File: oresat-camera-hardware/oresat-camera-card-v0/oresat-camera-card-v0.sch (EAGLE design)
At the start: 308 parts, among them J2 2-1734592-0, J5 DM3BT-DSF-PEJS, J6 J-SAMTEC-TFM-120-X1-XXX-D-RA, J8 3-1734592-64-1734592-0, Q1 DMP2240UDM, Q2 MMBT2907, Q3 MOSFET-PCH-SOT23-6, Q4 MOSFET-PCH-SOT23-6, Q5 PMV45EN, Q6 PMV45EN, Q7 DMP2240UDM, U1 OSD3358-512M-BSM, U11 SN74LVC8T245MPWREPPW24-M, U12 TCA9509DGKRDGK8-M, U13 TLVH431, U14 RCLAMP0504FB, U15 TLV70028QDDCRQ1, U16 RCLAMP0504FB, U2 TCAN330, U3 MAX7310ATE, U4 MAX4211CETE, U5 TPS62112, U6 CLVCH16T245MDGGREP, U8 SN74LVC1G07DCK, U9 TPS2051CDBVR, Y2 24MHz

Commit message: first draft finished
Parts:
- removed C40, C41, C42, C43: 0.1uF, oresat-rcl:C-EU0603-A-NOSILK
- removed D9: BLUE, SparkFun-LED:LED-BLUE0603
- removed J14: (no value), SparkFun-Connectors:CONN_03LONGPADS
- removed J15: (no value), SparkFun-Connectors:CONN_02PTH3
- removed U$2, U$4: MIC842, Q-Microchip-MIC842-Comparator:MIC842
- removed U16: RCLAMP0504FB, U-Semtec-RCLAMP0504FB:RCLAMP0504FB
- added C19, C20: 1uF, oresat-rcl:C-EU0603-A-NOSILK
- added C34: 0.1uF, oresat-rcl:C-EU0603-A-NOSILK
- added C8: 22u, oresat-rcl:C-EU0805-B-NOSILK
- added D3: GREEN, SparkFun-LED:LED-GREEN0603
- added J1: J-SAMTEC-TFM-120-X1-XXX-D-RA, J-Samtec-TFM-120-X1-XXX-D-RA:J-SAMTEC-TFM-120-X1-XXX-D-RA
- added J4: 3-1734592-64-1734592-0, J-TEConnectivity-X-1734592-X:3-1734592-64-1734592-0
- added JP7: JUMPER-SMT_3_1-NC_TRACE_SILK, SparkFun-Jumpers:JUMPER-SMT_3_1-NC_TRACE_SILK
- added Q8: PMV45EN, Tova:PMV45EN
- added TP143, TP144: TEST-POINT3X4, SparkFun-Connectors:TEST-POINT3X4
- added U7: TCA9509DGKRDGK8-M, U-TI-TCA9509DGKR-I2C_repeater:TCA9509DGKRDGK8-M
- C1: value 100n -> NP; device rcl_custom:C-EU0402-B-NOSILK -> oresat-rcl:C-EU0805-B-NOSILK; DIS Digi-Key -> (none); DPN 1276-1001-1-ND -> (none); MFR Samsung -> (none); MPN CL05B104KO5NNNC -> (none)
- C10: value 1u -> 0.1uF; DIS Digi-Key -> (none); DPN 1276-1001-1-ND -> (none); MFR Samsung -> (none); MPN CL05B104KO5NNNC -> (none)
- C11: DIS (none) -> Digi-Key; DPN (none) -> 1276-1001-1-ND; MFR (none) -> Samsung; MPN (none) -> CL05B104KO5NNNC
- C12: value 22u -> 0.1uF; device oresat-rcl:C-EU0805-B-NOSILK -> oresat-rcl:C-EU0603-A-NOSILK
- C13: value 22uF -> 0.1uF; device oresat-rcl:C-EUC1210 -> oresat-rcl:C-EU0603-A-NOSILK
- C14: value 0.1uF, 6.3V -> 0.1uF
- C15: value 18pF, 50V -> 0.1uF
- C17: DIS Digi-Key -> (none); DPN 1276-1001-1-ND -> (none); MFR Samsung -> (none); MPN CL05B104KO5NNNC -> (none)
- C18: value 18pF, 50V -> 2.2uF
- C2: device oresat-rcl:C-EU0603-A-NOSILK -> oresat-rcl:C-EU0805-B-NOSILK; DIS Digi-Key -> (none); DPN 1276-1001-1-ND -> (none); MFR Samsung -> (none); MPN CL05B104KO5NNNC -> (none)
- C21, C26: value 0.1uF -> 1uF
- C22: value 22uF -> 1uF; device oresat-rcl:C-EUC1210 -> oresat-rcl:C-EU0603-A-NOSILK
- C23: value 0.1uF -> 10uF
- C24, C27, C33: value 10uF -> 0.1uF
- C25: value 10uF -> 1uF
- C28: value 2.2uF -> 18pF, 50V
- C29: value 1uF -> 18pF, 50V
- C3: value 0.1uF -> 100n; DIS (none) -> Digi-Key; DPN (none) -> 1276-1001-1-ND; MFR (none) -> Samsung; MPN (none) -> CL05B104KO5NNNC
- C30, C32: value 1uF -> 0.1uF
- C31: value 1uF -> 1nF
- C35, C36: value 1uF -> 10uF
- C37, C38: value 0.1uF -> 22uF; device oresat-rcl:C-EU0603-A-NOSILK -> oresat-rcl:C-EUC1210
- C39: value 0.1uF -> 0.1uF, 6.3V
- C4: value NP -> 10u
- C6: value NP -> 1u; device oresat-rcl:C-EU0805-B-NOSILK -> oresat-rcl:C-EU0603-A-NOSILK; DIS (none) -> Digi-Key; DPN (none) -> 1276-1001-1-ND; MFR (none) -> Samsung; MPN (none) -> CL05B104KO5NNNC
- C7: value 10u -> NP; device oresat-rcl:C-EU0805-B-NOSILK -> oresat-rcl:C-EU0603-A-NOSILK; DIS (none) -> Digi-Key; DPN (none) -> 1276-1001-1-ND; MFR (none) -> Samsung; MPN (none) -> CL05B104KO5NNNC
- C9: value 1nF -> 10uF
- D1: value GREEN -> AMBER
- D4: value AMBER -> BLUE; device SparkFun-LED:LED-GREEN0603 -> SparkFun-LED:LED-BLUE0603
- D5: value GREEN -> BLUE; device SparkFun-LED:LED-GREEN0603 -> SparkFun-LED:LED-BLUE0603
- D8: value BLUE -> GREEN; device SparkFun-LED:LED-BLUE0603 -> SparkFun-LED:LED-GREEN0603
- J10, J11: device SparkFun-Connectors:CONN_05 -> SparkFun-Connectors:CONN_02PTH3
- J2: value 2-1734592-0 -> DM3BT-DSF-PEJS; device J-TEConnectivity-X-1734592-X:2-1734592-0 -> J-Hirose-DM3BT-DSF-PEJS:DM3BT-DSF-PEJS
- J3: device SparkFun-Connectors:CONN_02PTH3 -> SparkFun-Connectors:CONN_03LONGPADS
- J5: value DM3BT-DSF-PEJS -> (none); device J-Hirose-DM3BT-DSF-PEJS:DM3BT-DSF-PEJS -> SparkFun-Connectors:CONN_05
- J6: value J-SAMTEC-TFM-120-X1-XXX-D-RA -> (none); device J-Samtec-TFM-120-X1-XXX-D-RA:J-SAMTEC-TFM-120-X1-XXX-D-RA -> SparkFun-Connectors:CONN_05; MFR Samtec -> (none); MPN TFM-120-01-L-D-RA -> (none)
- J8: value 3-1734592-64-1734592-0 -> 2-1734592-0; device J-TEConnectivity-X-1734592-X:3-1734592-64-1734592-0 -> J-TEConnectivity-X-1734592-X:2-1734592-0
- Q3, Q4: value MOSFET-PCH-SOT23-6 -> MIC842; device Q-MOSFET-PCH-SOT23-6:MOSFET-PCH-SOT23-6 -> Q-Microchip-MIC842-Comparator:MIC842; MFR Diodes Inc -> (none); MPN DMP3050LVT-7 -> (none)
- Q6: value PMV45EN -> MOSFET-PCH-SOT23-6; device Tova:PMV45EN -> Q-MOSFET-PCH-SOT23-6:MOSFET-PCH-SOT23-6; MFR (none) -> Diodes Inc; MPN (none) -> DMP3050LVT-7
- Q7: value DMP2240UDM -> MOSFET-PCH-SOT23-6; device Q-MOSFET-PCH-dual-SOT23-6:MOSFET-PCH-SOT23-6 -> Q-MOSFET-PCH-SOT23-6:MOSFET-PCH-SOT23-6; MPN DMP2240UDM -> DMP3050LVT-7
- R1: value 2.7k -> 100; device rcl_custom:R-US_0402-B-NOSILK -> oresat-rcl:R-US_0603-A-NOSILK
- R11, R14, R5, R8, R9: device rcl_custom:R-US_0402-B-NOSILK -> oresat-rcl:R-US_0603-A-NOSILK
- R12: value 2.7k -> 10k; device rcl_custom:R-US_0402-B-NOSILK -> oresat-rcl:R-US_0603-A-NOSILK
- R13: value NP -> 10k; device rcl_custom:R-US_0402-B-NOSILK -> oresat-rcl:R-US_0603-A-NOSILK
- R15: value 10k -> NP; device rcl_custom:R-US_0402-B-NOSILK -> oresat-rcl:R-US_0603-A-NOSILK
- R16: value 47k -> NP; device rcl_custom:R-US_0402-B-NOSILK -> oresat-rcl:R-US_0603-A-NOSILK
- R17, R3: value 0 -> NP; DIS (none) -> Digi-Key; DPN (none) -> 1276-4275-1-ND; MFR (none) -> Samsung; MPN (none) -> RC1005F6653CS
- R18: value 47k -> 10k; device rcl_custom:R-US_0402-B-NOSILK -> oresat-rcl:R-US_0603-A-NOSILK
- R19, R20, R21, R22: value NP -> TBD; device rcl_custom:R-US_0402-B-NOSILK -> oresat-rcl:R-US_0603-A-NOSILK
- R2: value 2.7k -> NP; device rcl_custom:R-US_0402-B-NOSILK -> oresat-rcl:R-US_0603-A-NOSILK
- R23, R24: value NP -> 47k; device rcl_custom:R-US_0402-B-NOSILK -> oresat-rcl:R-US_0603-A-NOSILK
- R25: value 100 -> 10k; device rcl_custom:R-US_0402-B-NOSILK -> oresat-rcl:R-US_0603-A-NOSILK
- R26: value 10k -> 2.7k; device rcl_custom:R-US_0402-B-NOSILK -> oresat-rcl:R-US_0603-A-NOSILK
- R29: value 100m -> NP; device rcl:R-US_R1206 -> oresat-rcl:R-US_0603-A-NOSILK; DIS (none) -> Digi-Key; DPN (none) -> 1276-4275-1-ND; MFR (none) -> Samsung; MPN (none) -> RC1005F6653CS
- R30, R38: value 10k -> NP
- R31: value 0 -> NP
- R32: value NP -> 100m; device oresat-rcl:R-US_0603-A-NOSILK -> rcl:R-US_R1206; DIS Digi-Key -> (none); DPN 1276-4275-1-ND -> (none); MFR Samsung -> (none); MPN RC1005F6653CS -> (none)
- R33: value 0 -> 2.7k
- R34: value NP -> 10k
- R35, R63, R64: value 10k -> 0
- R36: value NP -> 0
- R39: value 1k -> 10k; device oresat-rcl:R-US_0603-A -> oresat-rcl:R-US_0603-A-NOSILK; DIS (none) -> Digi-Key; DPN (none) -> 1276-4275-1-ND; MFR (none) -> Samsung; MPN (none) -> RC1005F6653CS
- R4: value 100 -> NP; device rcl_custom:R-US_0402-B-NOSILK -> oresat-rcl:R-US_0603-A-NOSILK
- R40: value 1M, 1% -> 10k; device oresat-rcl:R-US_0603-A -> oresat-rcl:R-US_0603-A-NOSILK; DIS (none) -> Digi-Key; DPN (none) -> 1276-4275-1-ND; MFR (none) -> Samsung; MPN (none) -> RC1005F6653CS
- R41: value 10K -> 2.7k; device R-Panasonic-EXB_A10PXXXJ:EXB-A10P391JC_ARRAY_EXBA-M -> oresat-rcl:R-US_0603-A-NOSILK; DIS (none) -> Digi-Key; DPN (none) -> 1276-4275-1-ND; MFR (none) -> Samsung; MPN (none) -> RC1005F6653CS
- R42: value 1k -> 10K; device oresat-rcl:R-US_0603-A -> R-Panasonic-EXB_A10PXXXJ:EXB-A10P391JC_ARRAY_EXBA-M
- R43, R44: value 1k -> 4.7k; device oresat-rcl:R-US_0603-A -> oresat-rcl:R-US_0603-A-NOSILK
- R45: value 1k -> 10k; device oresat-rcl:R-US_0603-A -> oresat-rcl:R-US_0603-A-NOSILK
- R46, R47: device oresat-rcl:R-US_0603-A -> oresat-rcl:R-US_0603-A-NOSILK
- R48: value 10k -> 10K; device oresat-rcl:R-US_0603-A -> R-Panasonic-EXB_A10PXXXJ:EXB-A10P391JC_ARRAY_EXBA-M
- R49: value 10k -> 1k
- R50: value 10K -> 1k; device R-Panasonic-EXB_A10PXXXJ:EXB-A10P391JC_ARRAY_EXBA-M -> oresat-rcl:R-US_0603-A
- R51, R52: value 100K -> 1k; device R-Panasonic-EXB_A10PXXXJ:EXB-A10P391JC_ARRAY_EXBA-M -> oresat-rcl:R-US_0603-A
- R53: value 100K -> 10K
- R54: value NP -> 4.7k; device rcl_custom:R-US_0402-B-NOSILK -> oresat-rcl:R-US_0603-A-NOSILK; DIS Digi-Key -> (none); DPN 1276-4275-1-ND -> (none); MFR Samsung -> (none); MPN RC1005F6653CS -> (none)
- R55: value 4.75K -> 4.7k
- R56: value 4.75K -> 10k
- R58: value 10k -> 100K; device oresat-rcl:R-US_0603-A-NOSILK -> R-Panasonic-EXB_A10PXXXJ:EXB-A10P391JC_ARRAY_EXBA-M
- R59, R60: value 4.7k -> 100K; device oresat-rcl:R-US_0603-A-NOSILK -> R-Panasonic-EXB_A10PXXXJ:EXB-A10P391JC_ARRAY_EXBA-M
- R6: value NP -> 100; device rcl_custom:R-US_0402-B-NOSILK -> oresat-rcl:R-US_0603-A-NOSILK
- R61: value 4.7k -> 10k; device oresat-rcl:R-US_0603-A-NOSILK -> oresat-rcl:R-US_0603-A
- R62: value 4.7k -> 1M, 1%; device oresat-rcl:R-US_0603-A-NOSILK -> oresat-rcl:R-US_0603-A
- R65: value 10k -> 4.75K
- R66: value 10.0K -> 4.75K; device oresat-rcl:R-US_0603-A -> oresat-rcl:R-US_0603-A-NOSILK
- R67: value 40.2K -> 10k
- R68: value 499 -> 10k
- R69: value 10K -> 10k; device R-Panasonic-EXB_A10PXXXJ:EXB-A10P391JC_ARRAY_EXBA-M -> oresat-rcl:R-US_0603-A
- R7: value 10k -> 100
- R70: value 100 -> 1k; device rcl_custom:R-US_0402-B-NOSILK -> oresat-rcl:R-US_0603-A; DIS Digi-Key -> (none); DPN 1276-4275-1-ND -> (none); MFR Samsung -> (none); MPN RC1005F6653CS -> (none)
- R71: value 10k -> 499; device rcl_custom:R-US_0402-B-NOSILK -> oresat-rcl:R-US_0603-A; DIS Digi-Key -> (none); DPN 1276-4275-1-ND -> (none); MFR Samsung -> (none); MPN RC1005F6653CS -> (none)
- R72: value NP -> 40.2K; device rcl_custom:R-US_0402-B-NOSILK -> oresat-rcl:R-US_0603-A; DIS Digi-Key -> (none); DPN 1276-4275-1-ND -> (none); MFR Samsung -> (none); MPN RC1005F6653CS -> (none)
- R73: value NP -> 10.0K; device rcl_custom:R-US_0402-B-NOSILK -> oresat-rcl:R-US_0603-A; DIS Digi-Key -> (none); DPN 1276-4275-1-ND -> (none); MFR Samsung -> (none); MPN RC1005F6653CS -> (none)
- TP142: value TEST-POINT -> TEST-POINT3X4; device Tova:TEST-POINT -> SparkFun-Connectors:TEST-POINT3X4
- TP15: value TEST-POINT3X4 -> TEST-POINT; device SparkFun-Connectors:TEST-POINT3X4 -> Tova:TEST-POINT
- U1: value OSD3358-512M-BSM -> MAX7310ATE; device U-OSD3358-512M-BSM:OSD3358-512M-BSM -> U-Maxim-MAX7310-I2C-GPIO-expander:MAX7310; MFR (none) -> Maxim; MPN (none) -> MAX7310ATE
- U10: value (none) -> SN74LVC8T245MPWREPPW24-M; device U-Generic-eMMC-153pin:EMMC+RESET-BA -> U-TI-SN74LVC8T245MPWREP-8bit-TRX:SN74LVC8T245MPWREPPW24-M
- U11: value SN74LVC8T245MPWREPPW24-M -> RCLAMP0504FB; device U-TI-SN74LVC8T245MPWREP-8bit-TRX:SN74LVC8T245MPWREPPW24-M -> U-Semtec-RCLAMP0504FB:RCLAMP0504FB
- U12: value TCA9509DGKRDGK8-M -> RCLAMP0504FB; device U-TI-TCA9509DGKR-I2C_repeater:TCA9509DGKRDGK8-M -> U-Semtec-RCLAMP0504FB:RCLAMP0504FB
- U13: value TLVH431 -> TPS2051CDBVR; device U-TI-TLVH431-Shunt-Regulator:TLVH431 -> U-TI-TPS2051C:TPS2051CDBVR
- U14: value RCLAMP0504FB -> TLVH431; device U-Semtec-RCLAMP0504FB:RCLAMP0504FB -> U-TI-TLVH431-Shunt-Regulator:TLVH431
- U15: value TLV70028QDDCRQ1 -> SN74LVC1G07DCK; device U-TI-TLV70028QDDCRQ1-VoltageReg:TLV70028QDDCRQ1 -> U-TI-SN74LVC1G07DCK-Buffer:SN74LVC1G07DCK
- U2: value TCAN330 -> TPS62112; device U-TI-TCAN330-CAN-transceiver:TCAN330 -> U-TI-TPS6211x-SPS-buck:TPS6211X; MFR Texas Instruments -> TI; MPN TCAN330GDCNT -> TPS62111RSA
- U3: value MAX7310ATE -> MAX4211CETE; device U-Maxim-MAX7310-I2C-GPIO-expander:MAX7310 -> U-Maxim-MAX4211-power-monitor:MAX4211; MPN MAX7310ATE -> MAX4211CETE
- U4: value MAX4211CETE -> TCAN330; device U-Maxim-MAX4211-power-monitor:MAX4211 -> U-TI-TCAN330-CAN-transceiver:TCAN330; MFR Maxim -> Texas Instruments; MPN MAX4211CETE -> TCAN330GDCNT
- U5: value TPS62112 -> CLVCH16T245MDGGREP; device U-TI-TPS6211x-SPS-buck:TPS6211X -> U-TI-CLVCH16T245MDGxREP-16bit-TRX:CLVCH16T245MDGGREP; MFR TI -> (none); MPN TPS62111RSA -> (none)
- U6: value CLVCH16T245MDGGREP -> OSD3358-512M-BSM; device U-TI-CLVCH16T245MDGxREP-16bit-TRX:CLVCH16T245MDGGREP -> U-OSD3358-512M-BSM:OSD3358-512M-BSM
- U8: value SN74LVC1G07DCK -> (none); device U-TI-SN74LVC1G07DCK-Buffer:SN74LVC1G07DCK -> U-Generic-eMMC-153pin:EMMC+RESET-BA
- U9: value TPS2051CDBVR -> TLV70028QDDCRQ1; device U-TI-TPS2051C:TPS2051CDBVR -> U-TI-TLV70028QDDCRQ1-VoltageReg:TLV70028QDDCRQ1
- renumbered C44 to C16, CM4 to CM1, J12 to J7, J13 to J9, L2 to L1, Q2 to Q9, Y2 to Y1
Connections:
- new net N$100: C2.1, Q4.CIN, R20.1, R22.1
- new net N$101: C1.1, Q3.CIN, R19.1, R21.1
- new net N$102: JP7.2, U6B.USB1_ID
- new net USB_HO_ID: J8.4, JP7.1
- net !FAULT: now also Q8.D, R40.1, TP10.1, U1.IO2; no longer Q6.D, R38.1, TP8.1, U3.IO2
- net !OE_E: now also J4.26, U10.A5; no longer J8.26, U11.A5
- net !RESET_E: now also J4.24, U10.A3; no longer J8.24, U11.A3
- net !SD: now also J1.39, J1.40; no longer J6.39, J6.40
- net 2.8V: now also C14.1, C15.1, C17.1, C24.1, C26.1, R54.1, R55.1, U10.VCCA, U5.VCCB, U7.VCCB, U9.OUT; no longer C36.1, C39.1, C40.1, C41.1, C43.1, R59.1, R60.1, U11.VCCA, U12.VCCB, U15.OUT, U6.VCCB
- net 3.3V: now also C10.1, C11.2, C12.1, C13.1, C19.1, C20.1, C21.1, C22.1, C23.1, C25.1, C9.1, J2.VDD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; no longer C17.2, C26.1, C29.1, C30.1, C31.1, C32.1, C33.1, C35.1, C37.1, C38.1, C42.1, J5.VDD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
- net 5V: now also C8.1, R33.2, TP15.1, U2.FB; no longer C12.1, R2.2, TP17.1, U5.FB
- net 5V_IN: now also C37.1, U6A.VIN_AC@1, U6A.VIN_AC@2, U6A.VIN_AC@3; no longer C13.1, U1A.VIN_AC@1, U1A.VIN_AC@2, U1A.VIN_AC@3
- net AD0: now also R14.2, R15.1, R16.1, R17.2, U1.AD0; no longer R5.1, R6.2, R8.2, R9.1, U3.AD0
- net AD1: now also R10.1, R11.2, R8.2, R9.1, U1.AD1; no longer R11.1, R13.2, R14.2, R19.1, U3.AD1
- net AD2: now also R2.2, R3.1, R4.1, R5.2, U1.AD2; no longer R20.1, R21.2, R22.2, R23.1, U3.AD2
- net AGND: now also C31.2, C33.2, C34.2, R64.2, U6B.AGND_ADC; no longer C11.2, C3.2, C9.2, R17.2, U1B.AGND_ADC
- net BOOT0: now also U1.IO5; no longer U3.IO5
- net BUS_OE: now also R45.1, TP80.1, U5.!1OE, U5.!2OE, U6D.MII1_CRS; no longer R58.1, TP96.1, U1D.MII1_CRS, U6.!1OE, U6.!2OE
- net CAM_OE: now also TP81.1, U10.B5, U6D.MII1_COL; no longer TP97.1, U11.B5, U1D.MII1_COL
- net CAN1_H: now also J1.33, J1.34, TP143.1; no longer J6.33, J6.34
- net CAN1_L: now also J1.35, J1.36, TP144.1; no longer J6.35, J6.36
- net CAN2_H: now also J1.17, J1.18, U4.CANH; no longer J6.17, J6.18, U2.CANH
- net CAN2_L: now also J1.19, J1.20, U4.CANL; no longer J6.19, J6.20, U2.CANL
- net CB-RESET: now also R34.2, TP18.1, U1.IO4, U3.CIN2-; no longer R30.2, TP14.1, U3.IO4, U4.CIN2-
- net CB_CTRL: now also Q7.G, Q8.G, R39.1, TP14.1, U3.COUT1, U3.COUT2, U3.LE; no longer Q3.G, Q6.G, R35.1, TP3.1, U4.COUT1, U4.COUT2, U4.LE
- net CLK_EN: now also TP82.1, U10.B2, U6D.MII1_RX_CLK; no longer TP98.1, U11.B2, U1D.MII1_RX_CLK
- net CLK_EN_E: now also J4.23, U10.A2; no longer J8.23, U11.A2
- net D0_E: now also J4.12, U5.1B7; no longer J8.12, U6.1B7
- net D0_I: now also JP1.1, TP32.1, U5.1A7; no longer JP4.1, TP108.1, U6.1A7
- net D10_E: now also J4.16, U5.1B3; no longer J8.16, U6.1B3
- net D10_I: now also TP42.1, U5.1A3, U6C.MCASP0_AXR1; no longer TP118.1, U1C.MCASP0_AXR1, U6.1A3
- net D11_E: now also J4.17, U5.1B2; no longer J8.17, U6.1B2
- net D11_I: now also TP43.1, U5.1A2, U6C.MCASP0_AHCLKX; no longer TP119.1, U1C.MCASP0_AHCLKX, U6.1A2
- net D1_E: now also J4.11, U5.1B8; no longer J8.11, U6.1B8
- net D1_I: now also JP2.1, TP33.1, U5.1A8; no longer JP3.1, TP109.1, U6.1A8
- net D2_E: now also J4.10, U5.2B1; no longer J8.10, U6.2B1
- net D2_I: now also JP3.1, TP34.1, U5.2A1; no longer JP2.1, TP110.1, U6.2A1
- net D3_E: now also J4.9, U5.2B2; no longer J8.9, U6.2B2
- net D3_I: now also JP4.1, TP35.1, U5.2A2; no longer JP1.1, TP111.1, U6.2A2
- net D4_E: now also J4.8, U5.2B3; no longer J8.8, U6.2B3
- net D4_I: now also TP36.1, U5.2A3, U6C.MCASP0_ACLKX; no longer TP112.1, U1C.MCASP0_ACLKX, U6.2A3
- net D5_E: now also J4.7, U5.2B4; no longer J8.7, U6.2B4
- net D5_I: now also TP37.1, U5.2A4, U6C.MCASP0_FSX; no longer TP113.1, U1C.MCASP0_FSX, U6.2A4
- net D6_E: now also J4.6, U5.2B5; no longer J8.6, U6.2B5
- net D6_I: now also TP38.1, U5.2A5, U6C.MCASP0_AXR0; no longer TP114.1, U1C.MCASP0_AXR0, U6.2A5
- net D7_E: now also J4.13, U5.1B6; no longer J8.13, U6.1B6
- net D7_I: now also TP39.1, U5.1A6, U6C.MCASP0_AHCLKR; no longer TP115.1, U1C.MCASP0_AHCLKR, U6.1A6
- net D8_E: now also J4.14, U5.1B5; no longer J8.14, U6.1B5
- net D8_I: now also TP40.1, U5.1A5, U6C.MCASP0_ACLKR; no longer TP116.1, U1C.MCASP0_ACLKR, U6.1A5
- net D9_E: now also J4.15, U5.1B4; no longer J8.15, U6.1B4
- net D9_I: now also TP41.1, U5.1A4, U6C.MCASP0_FSR; no longer TP117.1, U1C.MCASP0_FSR, U6.1A4
- net FLASH: now also TP83.1, U5.1A1, U6D.MII1_TXD3; no longer TP99.1, U1D.MII1_TXD3, U6.1A1
- net FLASH_E: now also J4.28, U5.1B1; no longer J8.28, U6.1B1
- net GND: now also C1.2, C11.1, C15.2, C17.2, C18.2, C19.2, C2.2, C20.2, C3.1, C8.2, C9.2, D3.C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; no longer C1.1, C17.1, C28.2, C29.2, C31.2, C33.2, C40.2, C41.2, C42.2, C43.2, C7.2, D9.C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
- net HSYNC_E: now also J4.4, U5.2B7; no longer J8.4, U6.2B7
- net HSYNC_I: now also TP44.1, U5.2A7, U6C.GPMC_AD15; no longer TP120.1, U1C.GPMC_AD15, U6.2A7
- net I2C2_SCL: now also J4.21, R54.2, U7.SCLB; no longer J8.21, R60.2, U12.SCLB
- net I2C2_SDA: now also J4.22, R55.2, U7.SDAB; no longer J8.22, R59.2, U12.SDAB
- net INPUT_EN: now also R56.1, TP84.1, U10.!OE, U6D.MII1_RXD0; no longer R64.1, TP100.1, U11.!OE, U1D.MII1_RXD0
- net IOUT: now also R36.2, U3.IOUT; no longer R31.2, U4.IOUT
- net MAX4211-3V3: now also C6.1, TP6.1, U1.IO7, U3.VCC; no longer C5.1, TP10.1, U3.IO7, U4.VCC
- net N$1: now also C34.1, R63.2, TP116.1, U6B.SYS_ADC_1P8V; no longer C3.1, R3.2, TP15.1, U1B.SYS_ADC_1P8V
- net N$10: now also J2.CD#, R42.66, TP23.1, U6C.SPI0_CS1; no longer J5.CD#, R50.66, TP39.1, U1C.SPI0_CS1
- net N$11: now also U4.RXD, U6C.UART1_TXD; no longer U1C.UART1_TXD, U2.RXD
- net N$12: now also U4.TXD, U6C.UART1_RXD; no longer U1C.UART1_RXD, U2.TXD
- net N$13: now also TP21.1, U4.S; no longer TP44.1, U2.S
- net N$14: now also TP22.1, U4.SHDN; no longer TP42.1, U2.SHDN
- net N$15: now also JP4.2, U6C.MMC0_DAT0; no longer JP1.2, U1C.MMC0_DAT0
- net N$16: now also JP3.2, U6C.MMC0_DAT1; no longer JP2.2, U1C.MMC0_DAT1
- net N$17: now also JP2.2, U6C.MMC0_DAT2; no longer JP3.2, U1C.MMC0_DAT2
- net N$18: now also JP1.2, U6C.MMC0_DAT3; no longer JP4.2, U1C.MMC0_DAT3
- net N$19: now also R46.1, U5.1DIR, U5.2DIR; no longer R57.1, U6.1DIR, U6.2DIR
- net N$2: now also D7.A, R52.2; no longer D9.A, R45.2
- net N$20: now also JP6.2, R71.2, R73.2; no longer JP5.2, R66.2, R68.2
- net N$21: now also R47.1, U7.EN; no longer R63.1, U12.EN
- net N$22: now also R72.2, R73.1, U14.REF; no longer R66.1, R67.2, U13.REF
- net N$23: now also R71.1, U14.CATHODE; no longer R68.1, U13.CATHODE
- net N$24: now also R57.1, U10.DIR; no longer R65.1, U11.DIR
- net N$25: now also J3.2, U6C.UART0_TXD; no longer J14.2, U1C.UART0_TXD
- net N$26: now also JP6.1, TP131.1, U6A.SYS_VDD3_3P3V@1, U6A.SYS_VDD3_3P3V@2, U6A.SYS_VDD3_3P3V@3, U6A.SYS_VDD3_3P3V@4, U6A.SYS_VDD3_3P3V@5, U6A.SYS_VDD3_3P3V@6, U6A.SYS_VDD3_3P3V@7, U6A.SYS_VDD3_3P3V@8, U6A.VDDSHV1, U6A.VDDSHV2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; no longer JP5.1, TP29.1, U1A.SYS_VDD3_3P3V@1, U1A.SYS_VDD3_3P3V@2, U1A.SYS_VDD3_3P3V@3, U1A.SYS_VDD3_3P3V@4, U1A.SYS_VDD3_3P3V@5, U1A.SYS_VDD3_3P3V@6, U1A.SYS_VDD3_3P3V@7, U1A.SYS_VDD3_3P3V@8, U1A.VDDSHV1, U1A.VDDSHV2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
- net N$27: now also J3.1, U6C.UART0_RXD; no longer J14.1, U1C.UART0_RXD
- net N$270: now also D3.A, R41.1; no longer D1.A, R1.1
- net N$271: now also R33.1; no longer R2.1
- net N$28: now also TP26.1, U6C.SPI0_SCLK; no longer TP48.1, U1C.SPI0_SCLK
- net N$29: now also TP27.1, U6C.SPI0_D0; no longer TP47.1, U1C.SPI0_D0
- net N$3: now also U6B.AIN7, U6B.PMIC_MUX_OUT; no longer U1B.AIN7, U1B.PMIC_MUX_OUT
- net N$30: now also TP28.1, U6C.SPI0_D1; no longer TP46.1, U1C.SPI0_D1
- net N$31: now also TP29.1, U6C.SPI0_CS0; no longer TP45.1, U1C.SPI0_CS0
- net N$32: now also JP5.1, TP130.1, U6A.SYS_RTC_1P8V@1, U6A.SYS_RTC_1P8V@2; no longer JP6.1, TP28.1, U1A.SYS_RTC_1P8V@1, U1A.SYS_RTC_1P8V@2
- net N$33: now also TP30.1, U6C.XDMA_EVENT_INTR0; no longer TP49.1, U1C.XDMA_EVENT_INTR0
- net N$34: now also TP31.1, U6C.ECAP0_IN_PWM0_OUT; no longer TP50.1, U1C.ECAP0_IN_PWM0_OUT
- net N$35: now also TP60.1, U6C.GPMC_AD8; no longer TP51.1, U1C.GPMC_AD8
- net N$36: now also TP61.1, U6C.GPMC_AD9; no longer TP52.1, U1C.GPMC_AD9
- net N$37: now also TP62.1, U6C.GPMC_AD10; no longer TP53.1, U1C.GPMC_AD10
- net N$38: now also TP63.1, U6C.GPMC_AD11; no longer TP54.1, U1C.GPMC_AD11
- net N$385: now also R23.1, R24.1, TP9.1, U1.IO6; no longer R16.1, R18.1, TP5.1, U3.IO6
- net N$39: now also TP64.1, U6C.GPMC_AD12; no longer TP55.1, U1C.GPMC_AD12
- net N$4: now also J2.DAT2, JP2.3, R42.99; no longer J5.DAT2, JP3.3, R50.99
- net N$40: now also TP65.1, U6C.GPMC_AD13; no longer TP56.1, U1C.GPMC_AD13
- net N$401: now also TP126.1, U6A.VIN_BAT@1, U6A.VIN_BAT@2, U6A.VIN_BAT@3; no longer TP22.1, U1A.VIN_BAT@1, U1A.VIN_BAT@2, U1A.VIN_BAT@3
- net N$403: now also TP118.1, U6A.PMIC_BAT_SENSE; no longer TP23.1, U1A.PMIC_BAT_SENSE
- net N$404: now also TP117.1, U6A.PMIC_TS; no longer TP24.1, U1A.PMIC_TS
- net N$405: now also TP129.1, U6A.SYS_VDD2_3P3V@1, U6A.SYS_VDD2_3P3V@2; no longer TP27.1, U1A.SYS_VDD2_3P3V@1, U1A.SYS_VDD2_3P3V@2
- net N$407: now also JP5.2, R72.1, U14.ANODE; no longer JP6.2, R67.1, U13.ANODE
- net N$41: now also TP55.1, U6C.GPMC_BEN1; no longer TP57.1, U1C.GPMC_BEN1
- net N$42: now also TP56.1, U6C.GPMC_WAIT0; no longer TP58.1, U1C.GPMC_WAIT0
- net N$43: now also TP57.1, U6C.GPMC_WPN; no longer TP59.1, U1C.GPMC_WPN
- net N$44: now also TP24.1, U6C.UART0_CTSN; no longer TP60.1, U1C.UART0_CTSN
- net N$45: now also TP25.1, U6C.UART0_RTSN; no longer TP61.1, U1C.UART0_RTSN
- net N$46: now also TP90.1, U6D.LCD_PCLK; no longer TP62.1, U1D.LCD_PCLK
- net N$47: now also TP91.1, U6D.LCD_VSYNC; no longer TP63.1, U1D.LCD_VSYNC
- net N$479: now also Q1.1.S, R6.2; no longer Q7.1.S, R70.2
- net N$48: now also TP92.1, U6D.LCD_HSYNC; no longer TP64.1, U1D.LCD_HSYNC
- net N$480: now also Q1.1.G, Q3.COUT, R12.2, TP7.1; no longer Q7.1.G, R71.2, TP142.1, U$4.COUT
- net N$49: now also TP93.1, U6D.LCD_AC_BIAS_EN; no longer TP65.1, U1D.LCD_AC_BIAS_EN
- net N$499: now also TP132.1, U6A.SYS_VDD_1P8V@1, U6A.SYS_VDD_1P8V@2, U6A.SYS_VDD_1P8V@3, U6A.SYS_VDD_1P8V@4, U6A.SYS_VDD_1P8V@5, U6A.SYS_VDD_1P8V@6, U6A.SYS_VDD_1P8V@7, U6A.SYS_VDD_1P8V@8; no longer TP30.1, U1A.SYS_VDD_1P8V@1, U1A.SYS_VDD_1P8V@2, U1A.SYS_VDD_1P8V@3, U1A.SYS_VDD_1P8V@4, U1A.SYS_VDD_1P8V@5, U1A.SYS_VDD_1P8V@6, U1A.SYS_VDD_1P8V@7, U1A.SYS_VDD_1P8V@8
- net N$5: now also J2.DAT3/CS, JP1.3, R42.22; no longer J5.DAT3/CS, JP4.3, R50.22
- net N$50: now also TP77.1, U6D.RMII1_REF_CLK; no longer TP66.1, U1D.RMII1_REF_CLK
- net N$500: now also TP125.1, U6A.I2C0_SDA, U6A.PMIC_SDA; no longer TP31.1, U1A.I2C0_SDA, U1A.PMIC_SDA
- net N$503: now also TP124.1, U6A.I2C0_SCL, U6A.PMIC_SCL; no longer TP32.1, U1A.I2C0_SCL, U1A.PMIC_SCL
- net N$504: now also TP123.1, U6A.EXTINTN, U6A.PMIC_NINT; no longer TP33.1, U1A.EXTINTN, U1A.PMIC_NINT
- net N$51: now also TP78.1, U6D.MDC; no longer TP67.1, U1D.MDC
- net N$519: now also TP122.1, U6A.EXT_WAKEUP, U6A.PMIC_NWAKEUP; no longer TP34.1, U1A.EXT_WAKEUP, U1A.PMIC_NWAKEUP
- net N$52: now also TP79.1, U6D.MDIO; no longer TP68.1, U1D.MDIO
- net N$520: now also TP121.1, U6A.PMIC_LDO_PGOOD, U6A.RTC_PWRONRSTN; no longer TP35.1, U1A.PMIC_LDO_PGOOD, U1A.RTC_PWRONRSTN
- net N$524: now also TP120.1, U6A.PMIC_POWER_EN, U6A.PMIC_PWR_EN; no longer TP36.1, U1A.PMIC_POWER_EN, U1A.PMIC_PWR_EN
- net N$525: now also J10.2, U6A.PMIC_PB_IN; no longer J3.2, U1A.PMIC_PB_IN
- net N$529: now also TP119.1, U6A.PMIC_NRESET; no longer TP37.1, U1A.PMIC_NRESET
- net N$53: now also TP72.1, U6D.MII1_TX_CLK; no longer TP69.1, U1D.MII1_TX_CLK
- net N$530: now also U6B.TDO; no longer U1B.TDO
- net N$533: now also U6B.TCK; no longer U1B.TCK
- net N$534: now also U6B.TMS; no longer U1B.TMS
- net N$535: now also J6.1, U6D.LCD_DATA0; no longer J10.1, U1D.LCD_DATA0
- net N$54: now also TP73.1, U6D.MII1_TXD0; no longer TP70.1, U1D.MII1_TXD0
- net N$55: now also TP74.1, U6D.MII1_TXD1; no longer TP71.1, U1D.MII1_TXD1
- net N$56: now also TP75.1, U6D.MII1_TXD2; no longer TP72.1, U1D.MII1_TXD2
- net N$57: now also TP140.1, U6F.NC@1; no longer TP79.1, U1F.NC@1
- net N$575: now also D1.A, R26.1; no longer D4.A, R12.1
- net N$578: now also J6.2, U6D.LCD_DATA1; no longer J10.2, U1D.LCD_DATA1
- net N$579: now also Q1.2.S, R7.2; no longer Q1.1.S, R25.2
- net N$58: now also TP141.1, U6F.NC@2; no longer TP80.1, U1F.NC@2
- net N$580: now also Q1.2.G, Q4.COUT, R13.2, TP8.1; no longer Q1.1.G, R15.2, TP7.1, U$2.COUT
- net N$582: now also J6.3, U6D.LCD_DATA2; no longer J10.3, U1D.LCD_DATA2
- net N$583: now also J6.4, U6D.LCD_DATA3; no longer J10.4, U1D.LCD_DATA3
- net N$584: now also J6.5, U6D.LCD_DATA4; no longer J10.5, U1D.LCD_DATA4
- net N$585: now also R60.88, U6D.LCD_DATA5; no longer R53.88, U1D.LCD_DATA5
- net N$586: now also R60.66, U6D.LCD_DATA6; no longer R53.66, U1D.LCD_DATA6
- net N$587: now also R58.11, U6D.LCD_DATA8; no longer R52.11, U1D.LCD_DATA8
- net N$588: now also R58.99, U6D.LCD_DATA9; no longer R52.99, U1D.LCD_DATA9
- net N$589: now also R18.1, U1.!RESET; no longer R26.1, U3.!RESET
- net N$59: now also TP142.1, U6F.NC@3; no longer TP81.1, U1F.NC@3
- net N$590: now also Q6.G; no longer Q4.G
- net N$591: now also R58.88, U6D.LCD_DATA10; no longer R52.88, U1D.LCD_DATA10
- net N$592: now also R58.33, U6D.LCD_DATA11; no longer R52.33, U1D.LCD_DATA11
- net N$594: now also R58.77, U6D.LCD_DATA12; no longer R52.77, U1D.LCD_DATA12
- net N$595: now also R58.44, U6D.LCD_DATA13; no longer R52.44, U1D.LCD_DATA13
- net N$596: now also R36.1, R38.2, TP19.1, U3.CIN1+; no longer R31.1, R32.2, TP12.1, U4.CIN1+
- net N$597: now also R35.1, R37.2, TP17.1, U3.CIN1-; no longer R33.1, R34.2, TP11.1, U4.CIN1-
- net N$599: now also R35.2, U3.CIN2+, U3.REF; no longer R33.2, U4.CIN2+, U4.REF
- net N$6: now also J2.CMD/DI, R42.88, U6C.MMC0_CMD; no longer J5.CMD/DI, R50.88, U1C.MMC0_CMD
- net N$60: now also TP139.1, U6F.VPP; no longer TP78.1, U1F.VPP
- net N$601: now also R59.44, U6D.LCD_DATA14; no longer R51.44, U1D.LCD_DATA14
- net N$602: now also R58.66, U6D.LCD_DATA15; no longer R52.66, U1D.LCD_DATA15
- net N$603: now also C7.1, R30.2, R31.2; no longer C2.1, R36.2, R37.2
- net N$604: now also R31.1, U3.INHIBIT; no longer R37.1, U4.INHIBIT
- net N$609: now also R69.2, U6A.RTC_KALDO_ENN; no longer R46.2, U1A.RTC_KALDO_ENN
- net N$61: now also TP138.1, U6F.CAP_VDD_RTC; no longer TP77.1, U1F.CAP_VDD_RTC
- net N$610: now also J11.2, U6A.EEPROM_WP; no longer J15.2, U1A.EEPROM_WP
- net N$619: now also R67.2, U13.EN, U6B.USB1_DRVVBUS; no longer R47.2, U1B.USB1_DRVVBUS, U9.EN
- net N$62: now also TP137.1, U6F.VDDS_PLL; no longer TP76.1, U1F.VDDS_PLL
- net N$620: now also R68.1, U13.!FLT; no longer R48.1, U9.!FLT
- net N$621: now also U6B.TDI; no longer U1B.TDI
- net N$629: now also R58.22, U6D.LCD_DATA7; no longer R52.22, U1D.LCD_DATA7
- net N$63: now also TP136.1, U6F.VDD_MPU; no longer TP75.1, U1F.VDD_MPU
- net N$630: now also R60.11; no longer R53.11
- net N$631: now also R60.99; no longer R53.99
- net N$632: now also R60.22; no longer R53.22
- net N$633: now also R60.44; no longer R53.44
- net N$634: now also R60.77; no longer R53.77
- net N$635: now also J5.1, R59.11; no longer J11.1, R51.11
- net N$636: now also J5.2, R59.99; no longer J11.2, R51.99
- net N$637: now also J5.3, R59.88; no longer J11.3, R51.88
- net N$638: now also J5.4, R59.77; no longer J11.4, R51.77
- net N$639: now also J5.5, R59.66; no longer J11.5, R51.66
- net N$64: now also TP135.1, U6F.VDD_CORE; no longer TP74.1, U1F.VDD_CORE
- net N$640: now also C18.1, U8.VDDI; no longer C28.1, U10.VDDI
- net N$641: now also R48.66, U6C.GPMC_AD0, U8.D0; no longer R69.66, U10.D0, U1C.GPMC_AD0
- net N$642: now also R53.11, U6C.GPMC_AD1, U8.D1; no longer R41.11, U10.D1, U1C.GPMC_AD1
- net N$643: now also R53.99, U6C.GPMC_AD2, U8.D2; no longer R41.99, U10.D2, U1C.GPMC_AD2
- net N$644: now also R48.77, U6C.GPMC_AD3, U8.D3; no longer R69.77, U10.D3, U1C.GPMC_AD3
- net N$645: now also R48.44, U6C.GPMC_AD4, U8.D4; no longer R69.44, U10.D4, U1C.GPMC_AD4
- net N$646: now also R48.33, U6C.GPMC_AD5, U8.D5; no longer R69.33, U10.D5, U1C.GPMC_AD5
- net N$647: now also R53.88, U6C.GPMC_AD6, U8.D6; no longer R41.88, U10.D6, U1C.GPMC_AD6
- net N$648: now also R53.22, U6C.GPMC_AD7, U8.D7; no longer R41.22, U10.D7, U1C.GPMC_AD7
- net N$649: now also R48.22, U6C.GPMC_CSN2, U8.CMD; no longer R69.22, U10.CMD, U1C.GPMC_CSN2
- net N$65: now also TP134.1, U6F.VDDS_DDR; no longer TP73.1, U1F.VDDS_DDR
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
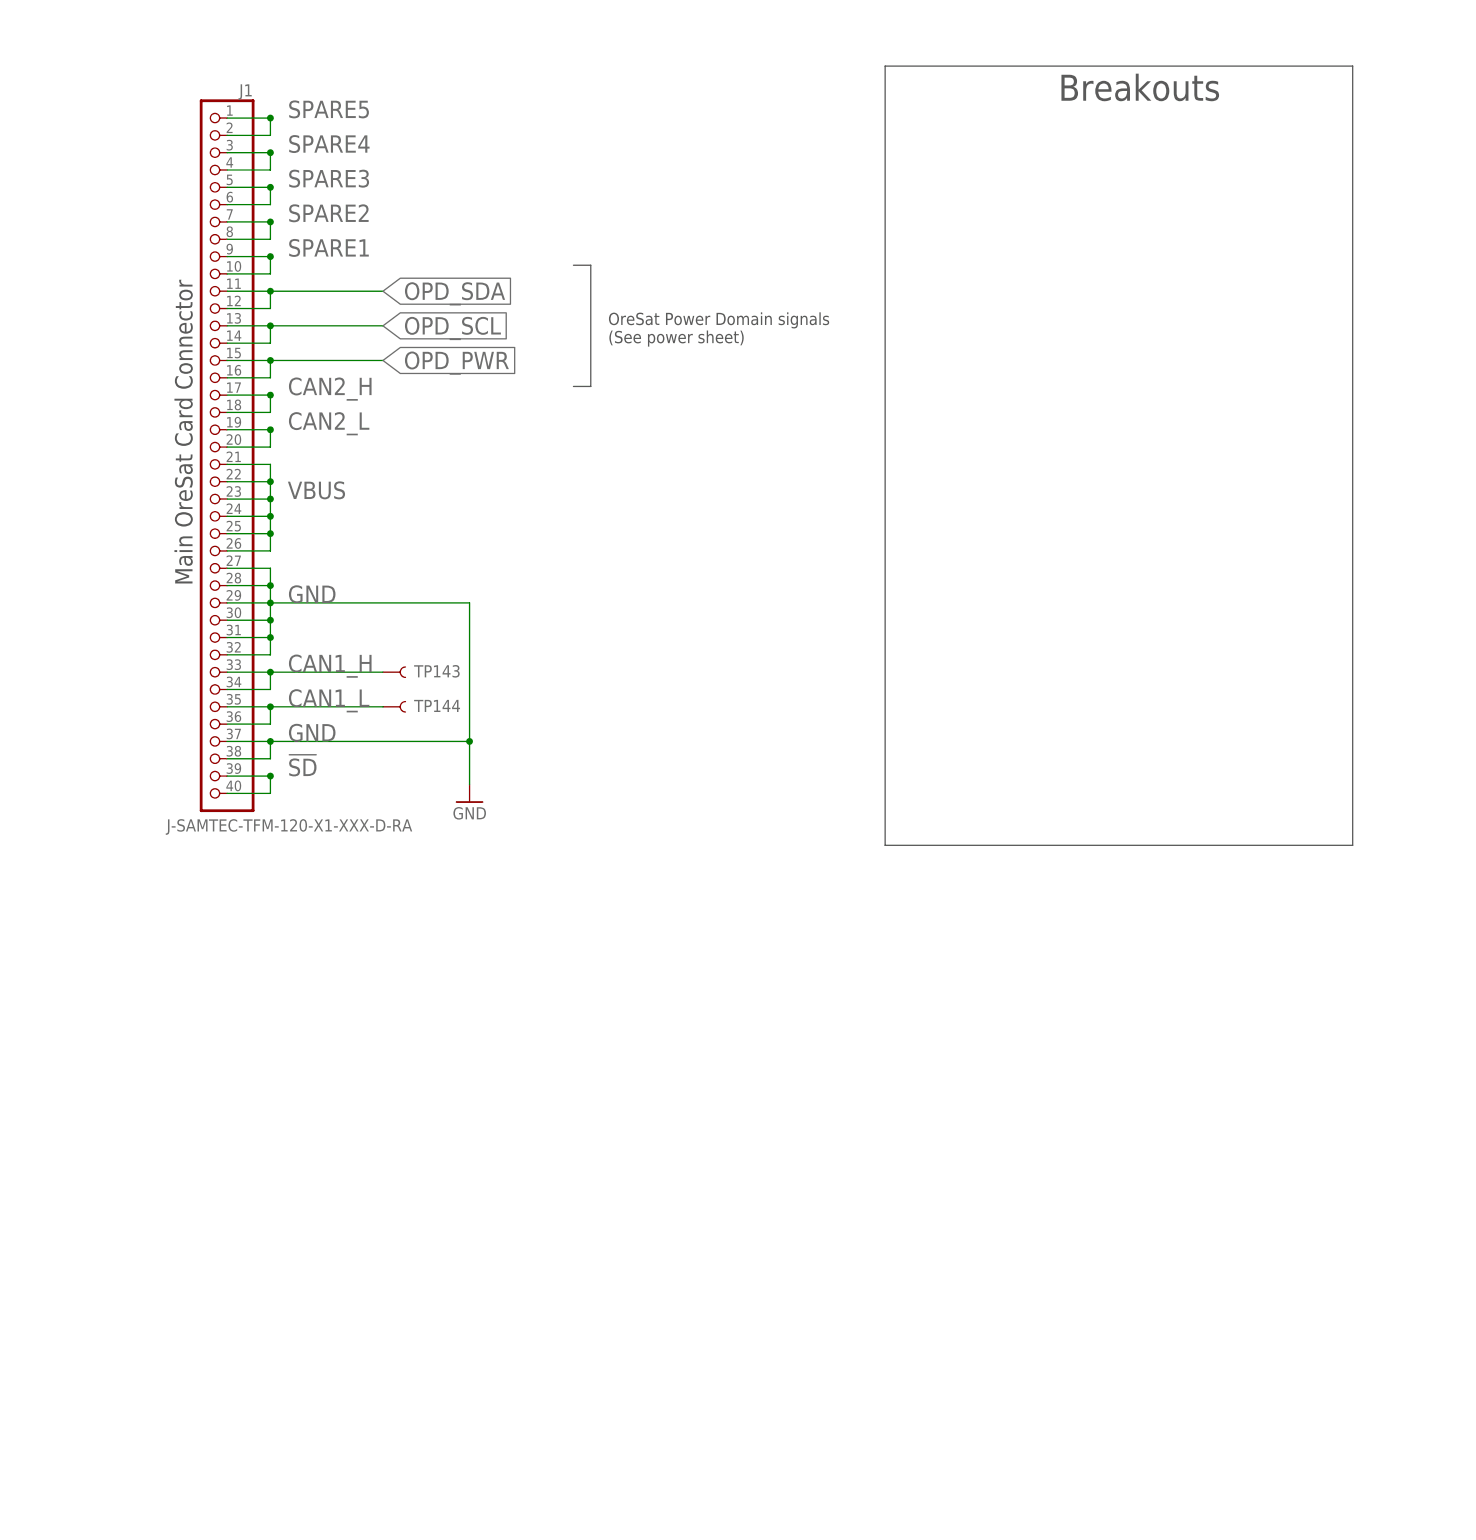
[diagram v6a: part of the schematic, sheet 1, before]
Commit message: ERC and DRC errors
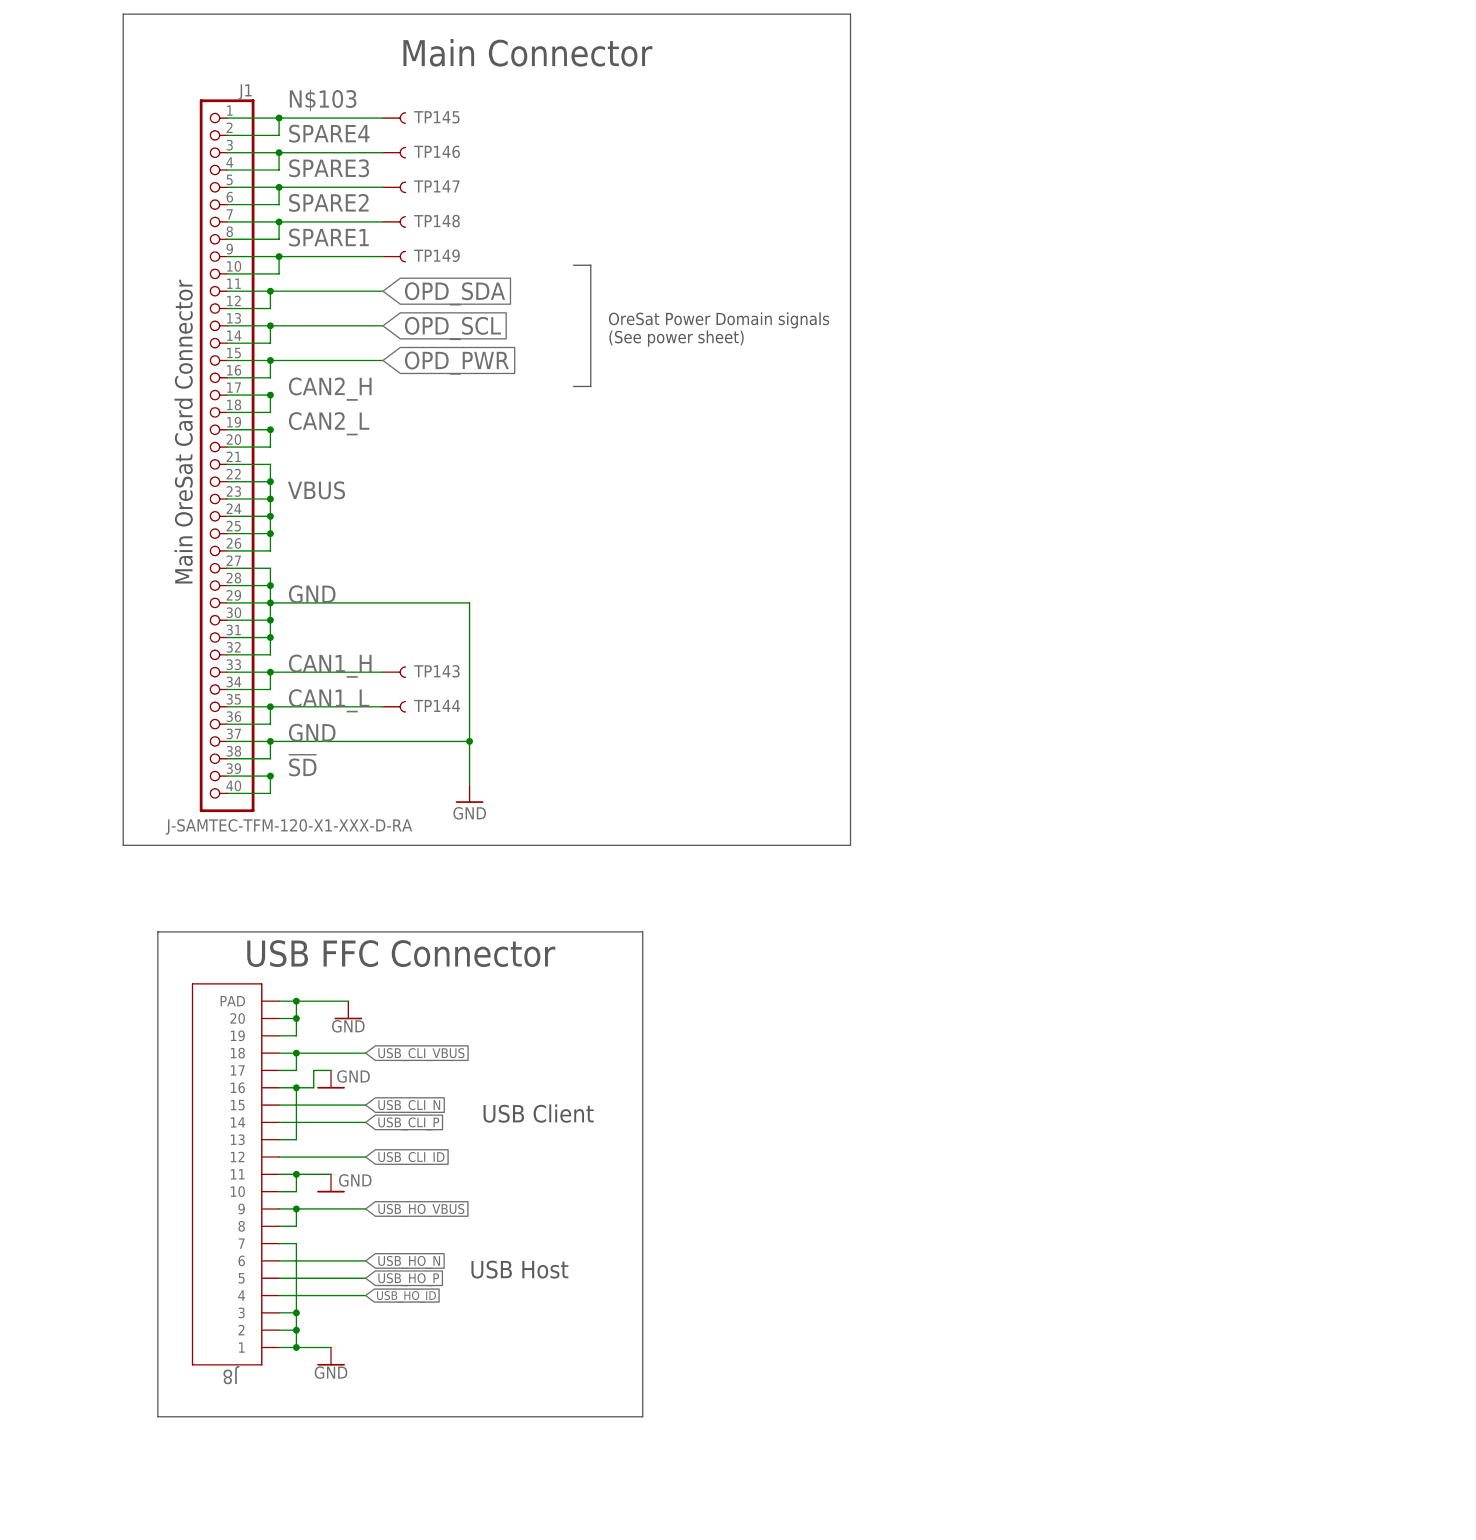
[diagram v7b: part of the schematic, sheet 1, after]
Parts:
- added TP145, TP146, TP147, TP148, TP149: TEST-POINT3X4, SparkFun-Connectors:TEST-POINT3X4
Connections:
- removed net SPARE5: J1.1, J1.2
- new net N$103: J1.1, J1.2, TP145.1
- net SPARE1: now also TP149.1
- net SPARE2: now also TP148.1
- net SPARE3: now also TP147.1
- net SPARE4: now also TP146.1
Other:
- note added: "Main Connector"
- note added: "USB FFC Connector"
- note removed: "Breakouts"
- note removed: "TODO cap between client shield and ground on breakout board"

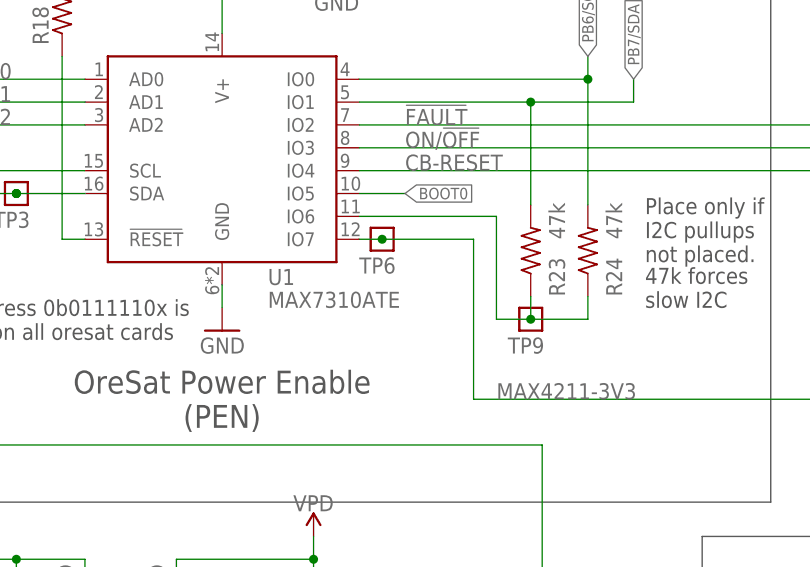
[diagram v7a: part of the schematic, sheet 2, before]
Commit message: broke out some pins
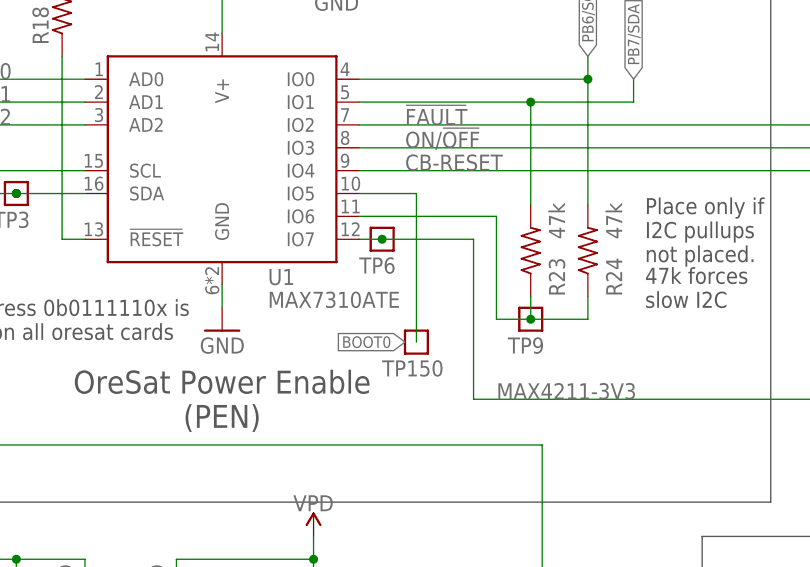
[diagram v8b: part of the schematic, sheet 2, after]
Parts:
- added TP150: TEST-POINT, Tova:TEST-POINT
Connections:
- net BOOT0: now also TP150.1
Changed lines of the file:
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@@
 <setting verticaltext="up"/>
 </settings>
-<grid distance="0.05" unitdist="inch" unit="inch" style="lines" multiple="1" display="no" altdistance="0.01" altunitdist="inch" altunit="inch"/>
+<grid distance="0.1" unitdist="inch" unit="inch" style="lines" multiple="1" display="yes" altdistance="0.05" altunitdist="inch" altunit="inch"/>
 <layers>
 <layer number="1" name="Top" color="4" fill="1" visible="no" active="no"/>
@@
 <part name="TP148" library="SparkFun-Connectors" deviceset="TEST-POINT" device="3X4"/>
 <part name="TP149" library="SparkFun-Connectors" deviceset="TEST-POINT" device="3X4"/>
+<part name="TP150" library="Tova" deviceset="TEST-POINT" device=""/>
 </parts>
 <sheets>
@@
 <attribute name="NAME" x="97.79" y="52.578" size="1.778" layer="95"/>
 </instance>
+<instance part="TP150" gate="G$1" x="153.67" y="135.89" smashed="yes" rot="R90">
+<attribute name="NAME" x="149.86" y="132.08" size="1.778" layer="95" font="vector"/>
+</instance>
 </instances>
 <busses>
@@
 <net name="BOOT0" class="0">
 <segment>
-<label x="152.4" y="152.4" size="1.27" layer="95" xref="yes"/>
-<wire x1="147.32" y1="152.4" x2="152.4" y2="152.4" width="0.1524" layer="91"/>
+<label x="152.4" y="135.89" size="1.27" layer="95" rot="R180" xref="yes"/>
+<wire x1="147.32" y1="152.4" x2="153.67" y2="152.4" width="0.1524" layer="91"/>
 <pinref part="U1" gate="G$1" pin="IO5"/>
-</segment>
-</net>
+<wire x1="153.67" y1="152.4" x2="153.67" y2="135.89" width="0.1524" layer="91"/>
+<pinref part="TP150" gate="G$1" pin="1"/>
+</segment>
+</net>
